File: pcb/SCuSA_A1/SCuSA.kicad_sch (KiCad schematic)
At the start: 6 parts, among them U101 XC6210B332MR, U102 AD8418

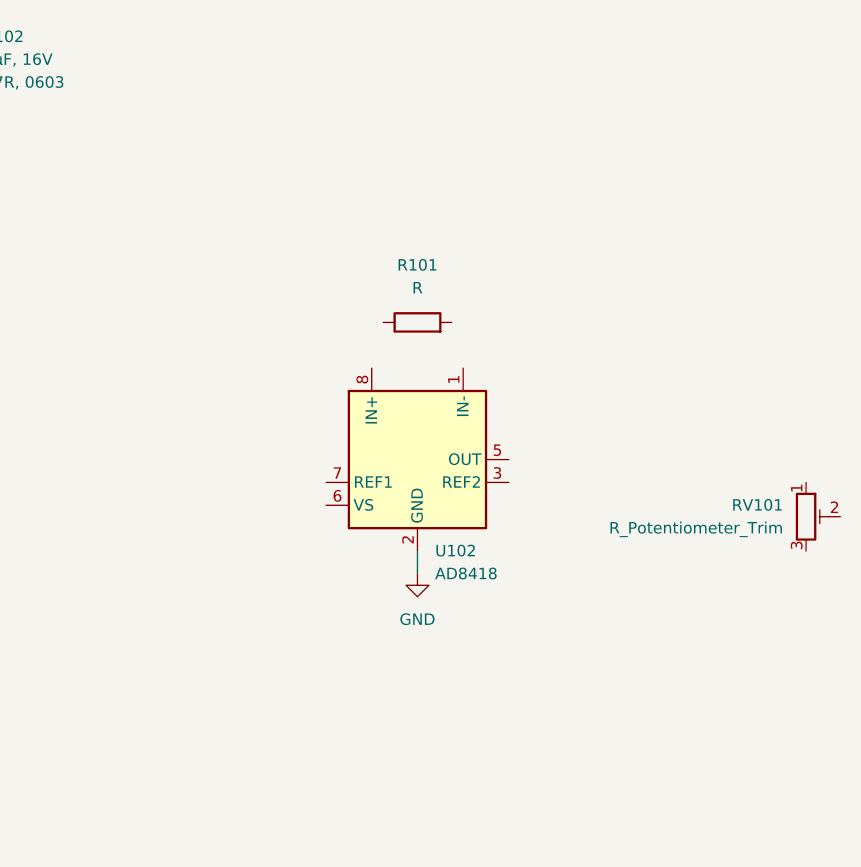
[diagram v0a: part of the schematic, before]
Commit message: Add alternative part simulation
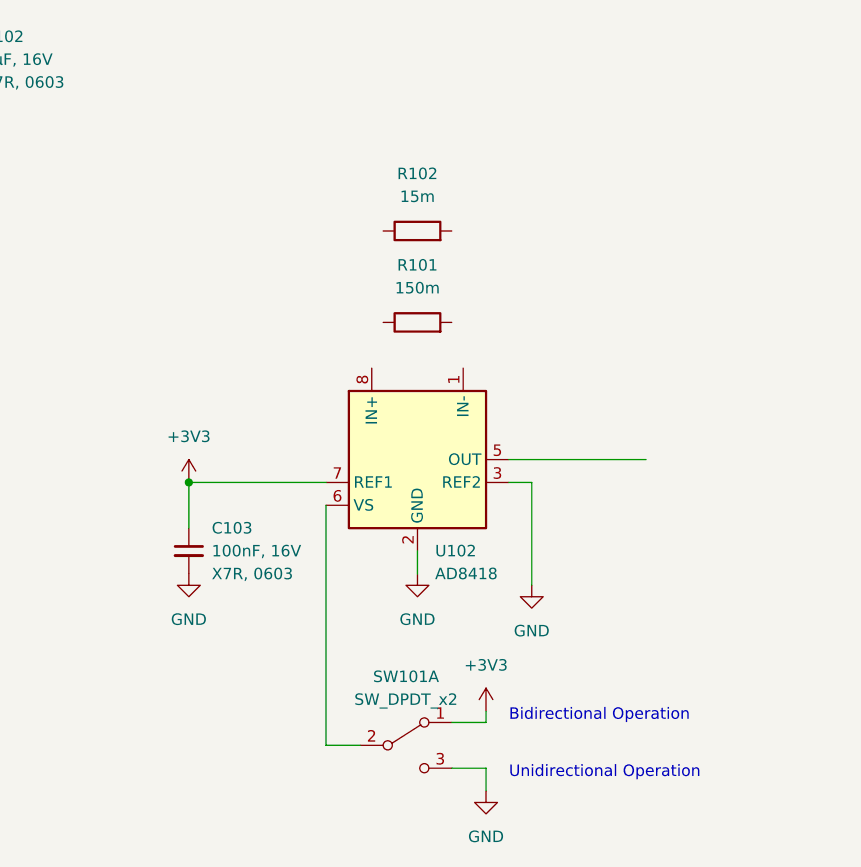
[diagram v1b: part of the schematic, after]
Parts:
- removed RV101: R_Potentiometer_Trim, symbol Device:R_Potentiometer_Trim
- added C103: 100nF,16V,X7R,0603, Capacitor_SMD:C_0603_1608Metric_Pad1.08x0.95mm_HandSolder, symbol Capacitor_User:100nF,16V,X7R,0603
- added R102: 15m, symbol Device:R
- added SW101: SW_DPDT_x2, symbol Switch:SW_DPDT_x2
- R101: value R -> 150m
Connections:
- net +3V3: now also U102.7 (REF1), C103.1, SW101.1 (A)
- net GND: now also U102.3 (REF2), C103.2, SW101.3 (C)
- net at U102.6 (VS): now also SW101.2 (B)
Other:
- note added: "Bidirectional Operation"
- note added: "Unidirectional Operation"
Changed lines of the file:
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@@
   (junction (at 88.9 60.96) (diameter 0) (color 0 0 0 0)
   )
+  (junction (at 139.7 113.03) (diameter 0) (color 0 0 0 0)
+  )
   (junction (at 114.3 60.96) (diameter 0) (color 0 0 0 0)
   )
+  (wire (pts (xy 168.91 139.7) (xy 172.72 139.7))
+    (stroke (width 0) (type default))
+  )
   (wire (pts (xy 165.1 120.65) (xy 165.1 123.19))
     (stroke (width 0) (type default))
@@
     (stroke (width 0) (type default))
   )
+  (wire (pts (xy 177.8 124.46) (xy 177.8 113.03))
+    (stroke (width 0) (type default))
+  )
+  (wire (pts (xy 168.91 144.78) (xy 172.72 144.78))
+    (stroke (width 0) (type default))
+  )
   (wire (pts (xy 72.39 60.96) (xy 88.9 60.96))
     (stroke (width 0) (type default))
   )
+  (wire (pts (xy 175.26 110.49) (xy 190.5 110.49))
+    (stroke (width 0) (type default))
+  )
+  (wire (pts (xy 158.75 142.24) (xy 154.94 142.24))
+    (stroke (width 0) (type default))
+  )
   (wire (pts (xy 72.39 68.58) (xy 72.39 73.66))
     (stroke (width 0) (type default))
@@
     (stroke (width 0) (type default))
   )
+  (wire (pts (xy 139.7 113.03) (xy 139.7 118.11))
+    (stroke (width 0) (type default))
+  )
+  (wire (pts (xy 172.72 139.7) (xy 172.72 138.43))
+    (stroke (width 0) (type default))
+  )
   (wire (pts (xy 72.39 63.5) (xy 72.39 60.96))
     (stroke (width 0) (type default))
   )
+  (wire (pts (xy 139.7 113.03) (xy 154.94 113.03))
+    (stroke (width 0) (type default))
+  )
   (wire (pts (xy 88.9 60.96) (xy 88.9 66.04))
     (stroke (width 0) (type default))
+  )
+  (wire (pts (xy 154.94 142.24) (xy 154.94 115.57))
+    (stroke (width 0) (type default))
+  )
+  (wire (pts (xy 172.72 144.78) (xy 172.72 147.32))
+    (stroke (width 0) (type default))
+  )
+  (wire (pts (xy 175.26 113.03) (xy 177.8 113.03))
+    (stroke (width 0) (type default))
+  )
+  (text "Bidirectional Operation" (at 175.26 139.7 0)
+    (effects (font (size 1.27 1.27)) (justify left bottom))
+  )
+  (text "Unidirectional Operation" (at 175.26 146.05 0)
+    (effects (font (size 1.27 1.27)) (justify left bottom))
+  )
+  (symbol (lib_id "Device:R") (at 165.1 85.09 90) (unit 1)
+    (in_bom yes) (on_board yes) (dnp no) (fields_autoplaced)
+    (property "Reference" "R102" (at 165.1 78.74 90)
+      (effects (font (size 1.27 1.27)))
+    )
+    (property "Value" "15m" (at 165.1 81.28 90)
+      (effects (font (size 1.27 1.27)))
+    )
+    (property "Footprint" "" (at 165.1 86.868 90)
+      (effects (font (size 1.27 1.27)) hide)
+    )
+    (property "Datasheet" "~" (at 165.1 85.09 0)
+      (effects (font (size 1.27 1.27)) hide)
+    )
+    (pin "1")
+    (pin "2")
+    (instances
+      (project "SCuSA"
+        (path "/7c524ebf-103a-4dc7-9ca9-e5a941b364b9"
+          (reference "R102") (unit 1)
+        )
+      )
+    )
   )
   (symbol (lib_id "Amplifier_Current:AD8418") (at 165.1 110.49 0) (unit 1)
@@
     )
   )
+  (symbol (lib_id "power:GND") (at 177.8 124.46 0) (unit 1)
+    (in_bom yes) (on_board yes) (dnp no) (fields_autoplaced)
+    (property "Reference" "#PWR0108" (at 177.8 130.81 0)
+      (effects (font (size 1.27 1.27)) hide)
+    )
+    (property "Value" "GND" (at 177.8 129.54 0)
+      (effects (font (size 1.27 1.27)))
+    )
+    (property "Footprint" "" (at 177.8 124.46 0)
+      (effects (font (size 1.27 1.27)) hide)
+    )
+    (property "Datasheet" "" (at 177.8 124.46 0)
+      (effects (font (size 1.27 1.27)) hide)
+    )
+    (pin "1")
+    (instances
+      (project "SCuSA"
+        (path "/7c524ebf-103a-4dc7-9ca9-e5a941b364b9"
+          (reference "#PWR0108") (unit 1)
+        )
+      )
+    )
+  )
+  (symbol (lib_id "power:+3V3") (at 139.7 113.03 0) (unit 1)
+    (in_bom yes) (on_board yes) (dnp no) (fields_autoplaced)
+    (property "Reference" "#PWR0106" (at 139.7 116.84 0)
+      (effects (font (size 1.27 1.27)) hide)
+    )
+    (property "Value" "+3V3" (at 139.7 107.95 0)
+      (effects (font (size 1.27 1.27)))
+    )
+    (property "Footprint" "" (at 139.7 113.03 0)
+      (effects (font (size 1.27 1.27)) hide)
+    )
+    (property "Datasheet" "" (at 139.7 113.03 0)
+      (effects (font (size 1.27 1.27)) hide)
+    )
+    (pin "1")
+    (instances
+      (project "SCuSA"
+        (path "/7c524ebf-103a-4dc7-9ca9-e5a941b364b9"
+          (reference "#PWR0106") (unit 1)
+        )
+      )
+    )
+  )
   (symbol (lib_id "power:GND") (at 101.6 73.66 0) (unit 1)
     (in_bom yes) (on_board yes) (dnp no) (fields_autoplaced)
@@
     )
   )
-  (symbol (lib_id "Device:R_Potentiometer_Trim") (at 208.28 116.84 0) (unit 1)
-    (in_bom yes) (on_board yes) (dnp no) (fields_autoplaced)
-    (property "Reference" "RV101" (at 205.74 115.57 0)
-      (effects (font (size 1.27 1.27)) (justify right))
-    )
-    (property "Value" "R_Potentiometer_Trim" (at 205.74 118.11 0)
-      (effects (font (size 1.27 1.27)) (justify right))
-    )
-    (property "Footprint" "" (at 208.28 116.84 0)
-      (effects (font (size 1.27 1.27)) hide)
-    )
-    (property "Datasheet" "~" (at 208.28 116.84 0)
-      (effects (font (size 1.27 1.27)) hide)
-    )
-    (pin "1")
-    (pin "2")
-    (pin "3")
-    (instances
-      (project "SCuSA"
-        (path "/7c524ebf-103a-4dc7-9ca9-e5a941b364b9"
-          (reference "RV101") (unit 1)
+  (symbol (lib_id "power:+3V3") (at 172.72 138.43 0) (unit 1)
+    (in_bom yes) (on_board yes) (dnp no) (fields_autoplaced)
+    (property "Reference" "#PWR0109" (at 172.72 142.24 0)
+      (effects (font (size 1.27 1.27)) hide)
+    )
+    (property "Value" "+3V3" (at 172.72 133.35 0)
+      (effects (font (size 1.27 1.27)))
+    )
+    (property "Footprint" "" (at 172.72 138.43 0)
+      (effects (font (size 1.27 1.27)) hide)
+    )
+    (property "Datasheet" "" (at 172.72 138.43 0)
+      (effects (font (size 1.27 1.27)) hide)
+    )
+    (pin "1")
+    (instances
+      (project "SCuSA"
+        (path "/7c524ebf-103a-4dc7-9ca9-e5a941b364b9"
+          (reference "#PWR0109") (unit 1)
+        )
+      )
+    )
+  )
+  (symbol (lib_id "power:GND") (at 139.7 123.19 0) (unit 1)
+    (in_bom yes) (on_board yes) (dnp no) (fields_autoplaced)
+    (property "Reference" "#PWR0107" (at 139.7 129.54 0)
+      (effects (font (size 1.27 1.27)) hide)
+    )
+    (property "Value" "GND" (at 139.7 128.27 0)
+      (effects (font (size 1.27 1.27)))
+    )
+    (property "Footprint" "" (at 139.7 123.19 0)
+      (effects (font (size 1.27 1.27)) hide)
+    )
+    (property "Datasheet" "" (at 139.7 123.19 0)
+      (effects (font (size 1.27 1.27)) hide)
+    )
+    (pin "1")
+    (instances
+      (project "SCuSA"
+        (path "/7c524ebf-103a-4dc7-9ca9-e5a941b364b9"
+          (reference "#PWR0107") (unit 1)
         )
       )
@@
       (effects (font (size 1.27 1.27)))
     )
-    (property "Value" "R" (at 165.1 91.44 90)
+    (property "Value" "150m" (at 165.1 91.44 90)
       (effects (font (size 1.27 1.27)))
     )
@@
         )
       )
+    )
+  )
+  (symbol (lib_id "Switch:SW_DPDT_x2") (at 163.83 142.24 0) (unit 1)
+    (in_bom yes) (on_board yes) (dnp no) (fields_autoplaced)
+    (property "Reference" "SW101" (at 163.83 134.62 0)
+      (effects (font (size 1.27 1.27)))
+    )
+    (property "Value" "SW_DPDT_x2" (at 163.83 137.16 0)
+      (effects (font (size 1.27 1.27)))
+    )
+    (property "Footprint" "" (at 163.83 142.24 0)
+      (effects (font (size 1.27 1.27)) hide)
+    )
+    (property "Datasheet" "~" (at 163.83 142.24 0)
+      (effects (font (size 1.27 1.27)) hide)
+    )
+    (pin "1")
+    (pin "2")
+    (pin "3")
+    (pin "4")
+    (pin "5")
+    (pin "6")
+    (instances
+      (project "SCuSA"
+        (path "/7c524ebf-103a-4dc7-9ca9-e5a941b364b9"
+          (reference "SW101") (unit 1)
+        )
+      )
+    )
+  )
+  (symbol (lib_id "power:GND") (at 172.72 147.32 0) (unit 1)
+    (in_bom yes) (on_board yes) (dnp no) (fields_autoplaced)
+    (property "Reference" "#PWR0110" (at 172.72 153.67 0)
+      (effects (font (size 1.27 1.27)) hide)
+    )
+    (property "Value" "GND" (at 172.72 152.4 0)
+      (effects (font (size 1.27 1.27)))
+    )
+    (property "Footprint" "" (at 172.72 147.32 0)
+      (effects (font (size 1.27 1.27)) hide)
+    )
+    (property "Datasheet" "" (at 172.72 147.32 0)
+      (effects (font (size 1.27 1.27)) hide)
+    )
+    (pin "1")
+    (instances
+      (project "SCuSA"
+        (path "/7c524ebf-103a-4dc7-9ca9-e5a941b364b9"
+          (reference "#PWR0110") (unit 1)
+        )
+      )
+    )
+  )
+  (symbol (lib_id "Capacitor_User:100nF,16V,X7R,0603") (at 139.7 120.65 0) (unit 1)
+    (in_bom yes) (on_board yes) (dnp no) (fields_autoplaced)
+    (property "Reference" "C103" (at 142.24 118.1163 0)
+      (effects (font (size 1.27 1.27)) (justify left))
+    )
+    (property "Value" "100nF,16V,X7R,0603" (at 142.24 125.73 0)
+      (effects (font (size 1.27 1.27)) (justify left) hide)
+    )
+    (property "Footprint" "Capacitor_SMD:C_0603_1608Metric_Pad1.08x0.95mm_HandSolder" (at 140.97 132.08 0)
+      (effects (font (size 1.27 1.27)) hide)
+    )
+    (property "Datasheet" "~" (at 139.7 120.65 0)
+      (effects (font (size 1.27 1.27)) hide)
+    )
+    (property "Pretty Value 1" "100nF, 16V" (at 142.24 120.6563 0)
+      (effects (font (size 1.27 1.27)) (justify left))
+    )
+    (property "Pretty Value 2" "X7R, 0603" (at 142.24 123.1963 0)
+      (effects (font (size 1.27 1.27)) (justify left))
+    )
+    (pin "1")
+    (pin "2")
+    (instances
+      (project "SCuSA"
+        (path "/7c524ebf-103a-4dc7-9ca9-e5a941b364b9"
+          (reference "C103") (unit 1)
+        )
+      )

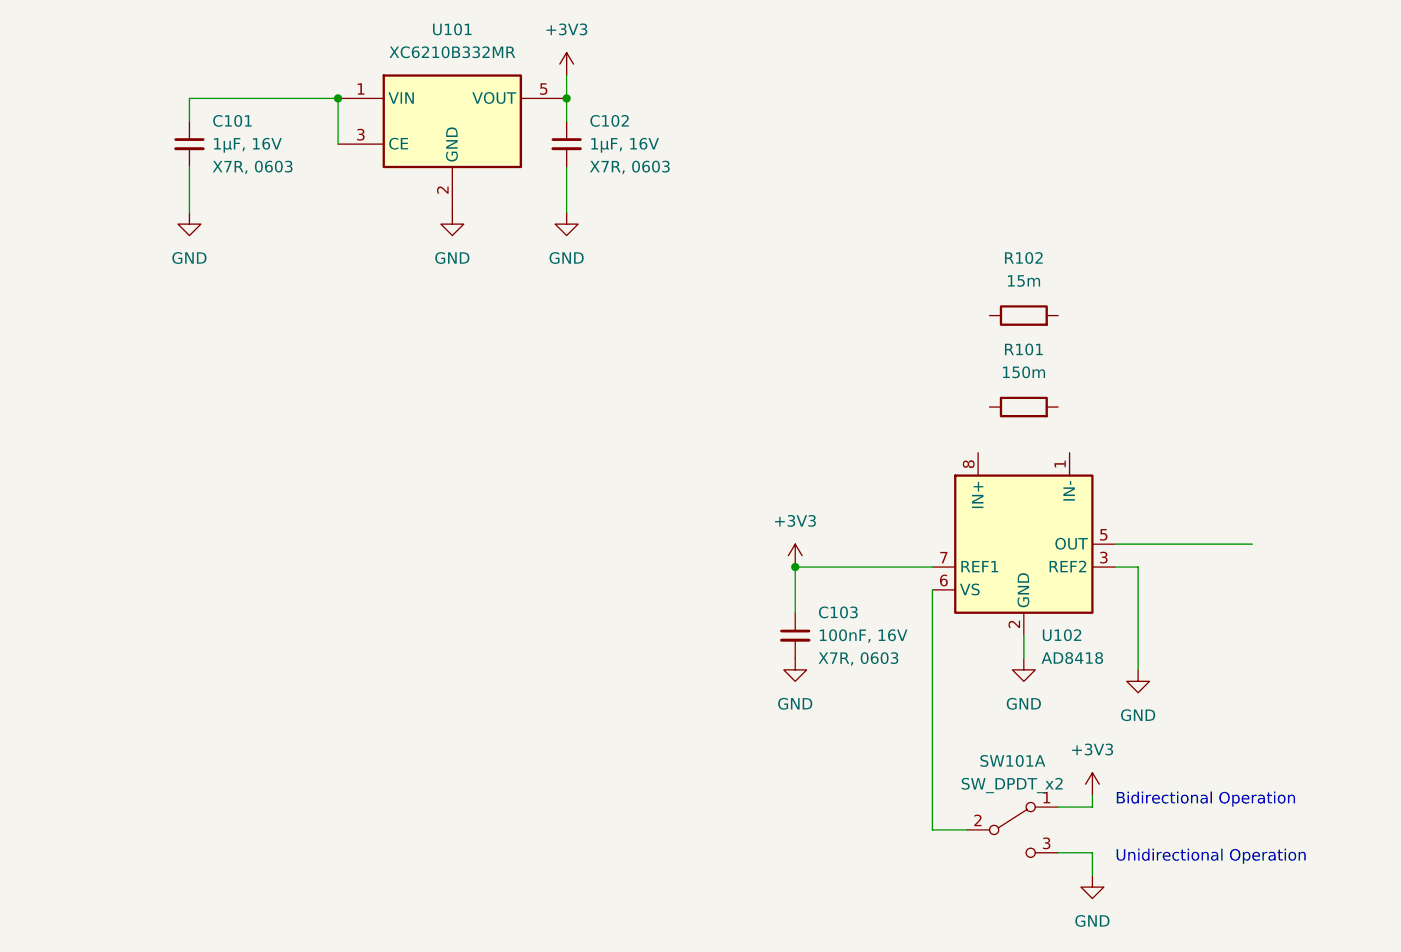
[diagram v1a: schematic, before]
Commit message: Switch to LM27762
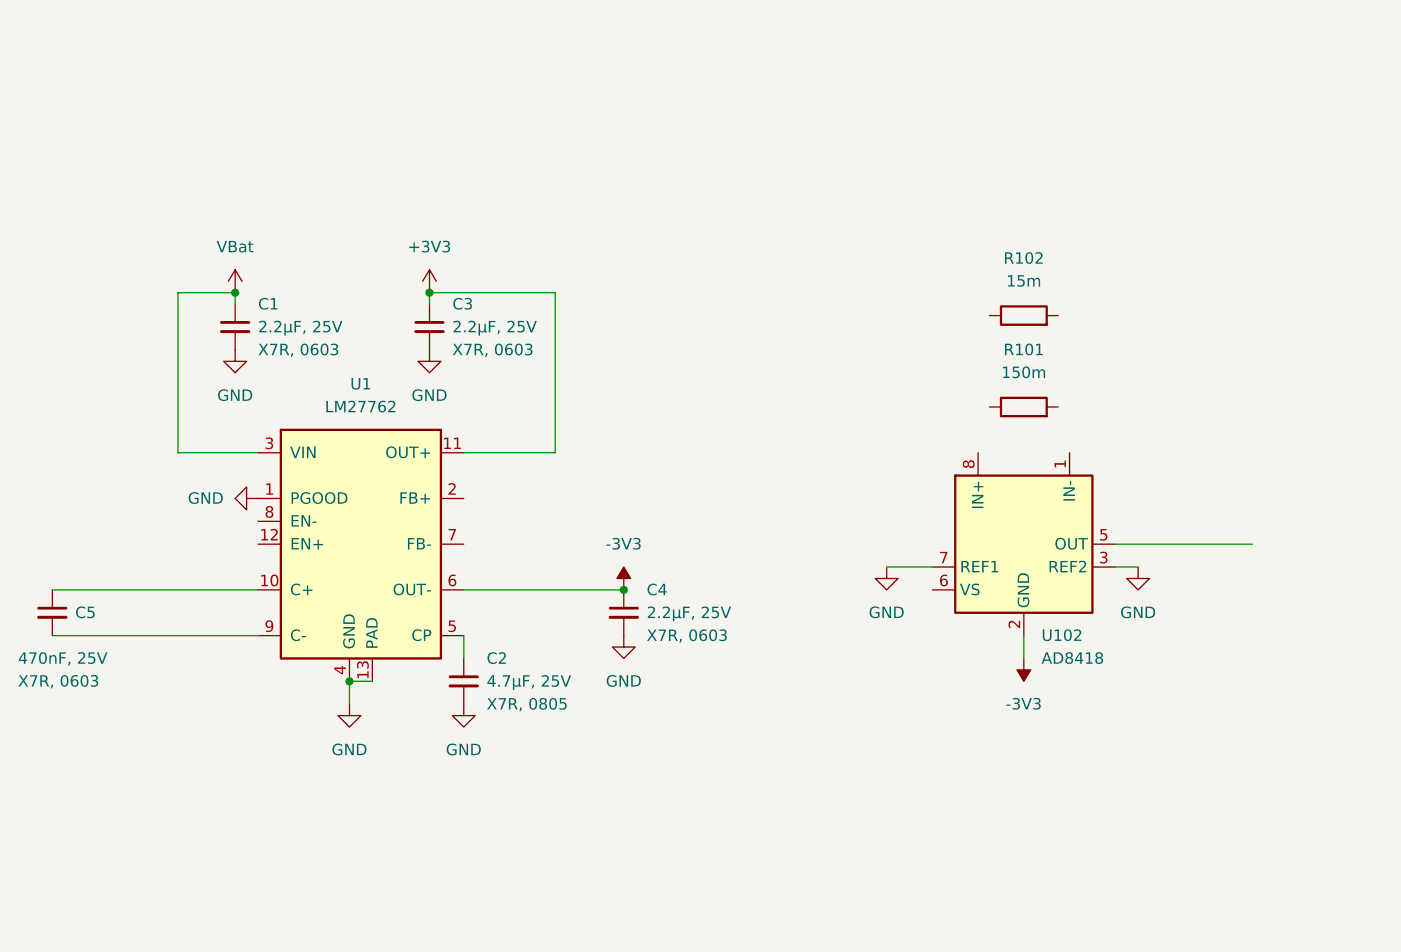
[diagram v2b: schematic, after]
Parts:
- removed C101, C102: 1uF,16V,X7R,0603, Capacitor_SMD:C_0603_1608Metric_Pad1.08x0.95mm_HandSolder, symbol Capacitor_User:1uF,16V,X7R,0603
- removed C103: 100nF,16V,X7R,0603, Capacitor_SMD:C_0603_1608Metric_Pad1.08x0.95mm_HandSolder, symbol Capacitor_User:100nF,16V,X7R,0603
- removed SW101: SW_DPDT_x2, symbol Switch:SW_DPDT_x2
- removed U101: XC6210B332MR, Package_TO_SOT_SMD:SOT-23-5, symbol Regulator_Linear:XC6210B332MR
- added C1, C3, C4: 2.2uF,25V,X7R,0603, Capacitor_SMD:C_0603_1608Metric_Pad1.08x0.95mm_HandSolder, symbol Capacitor_User:2.2uF,25V,X7R,0603
- added C2: 4.7uF,25V,X7R,0805, Capacitor_SMD:C_0805_2012Metric_Pad1.18x1.45mm_HandSolder, symbol Capacitor_User:4.7uF,25V,X7R,0805
- added C5: 470nF,25V,X7R,0603, Capacitor_SMD:C_0603_1608Metric_Pad1.08x0.95mm_HandSolder, symbol Capacitor_User:470nF,25V,X7R,0603
- added U1: LM27762, Package_SON:WSON-12-1EP_3x2mm_P0.5mm_EP1x2.65_ThermalVias, symbol Regulator_SwitchedCapacitor:LM27762
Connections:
- net +3V3: now also C3.1, U1.11 (OUT+); no longer U102.7 (REF1)
- net GND: now also U102.7 (REF1), C1.2, C2.2, C3.2, C4.2, U1.1 (PGOOD), U1.13 (PAD), U1.4 (GND); no longer U102.2 (GND)
- new net: C5.1, U1.10 (C+)
- new net: C2.1, U1.5 (CP)
- new net: C5.2, U1.9 (C-)
- new net -3V3: C4.1, U1.6 (OUT-), U102.2 (GND)
- new net VBat: C1.1, U1.3 (VIN)
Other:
- note removed: "Bidirectional Operation"
- note removed: "Unidirectional Operation"
